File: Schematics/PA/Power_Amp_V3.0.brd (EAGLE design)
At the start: 50.5 x 78.1 mm, 109 parts, among them J1 4_PIN_AMPCONN, J10 OSTVN03A150, J11 OSTVN03A150, J12 OSTVN03A150, J13 OSTVN03A150, J14 OSTVN03A150, J2 1984633, J3 2TERMINAL_SPEAKER, J4 2TERMINAL_SPEAKER, J5 2TERMINAL_SPEAKER, J6 OSTVN03A150, J7 OSTVN03A150, J8 OSTVN03A150, J9 OSTVN03A150, U1 LME49830, U2 LME49830, U3 LME49830

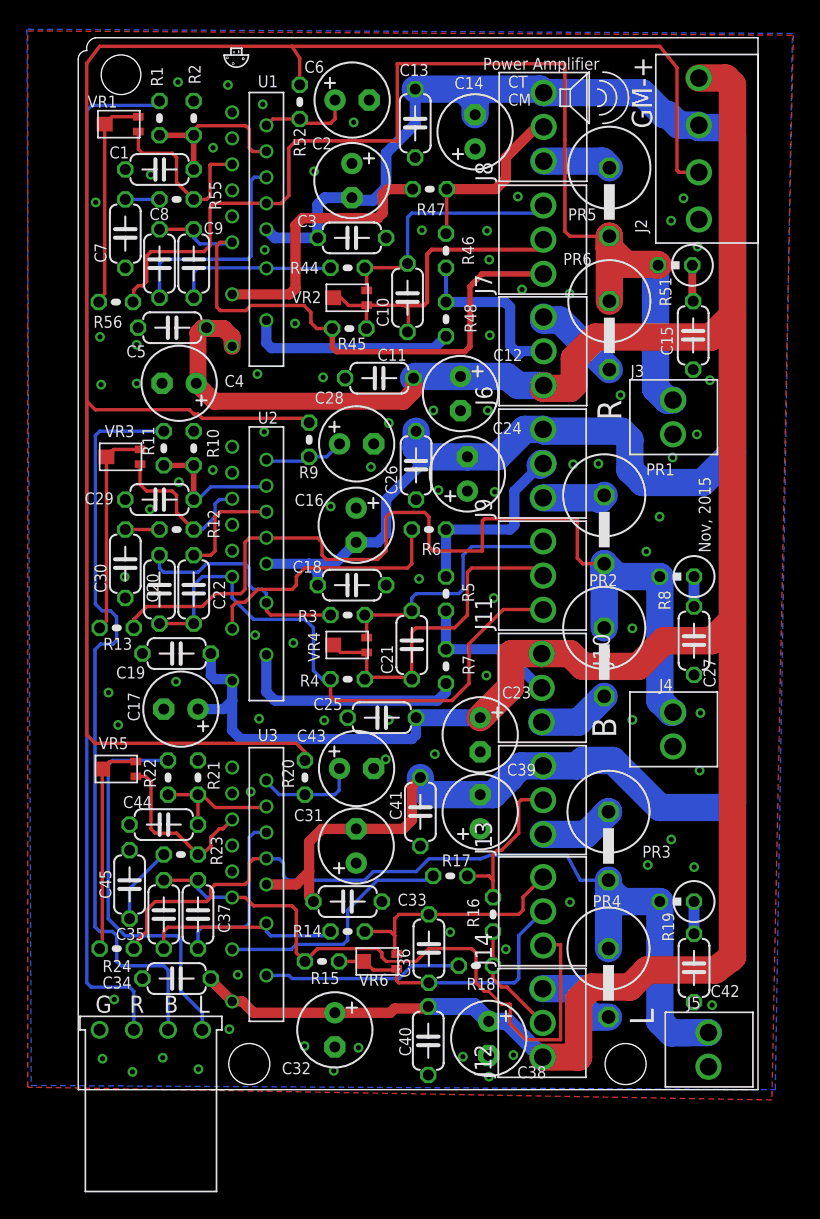
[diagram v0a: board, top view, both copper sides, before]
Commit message: small changes to silk screen
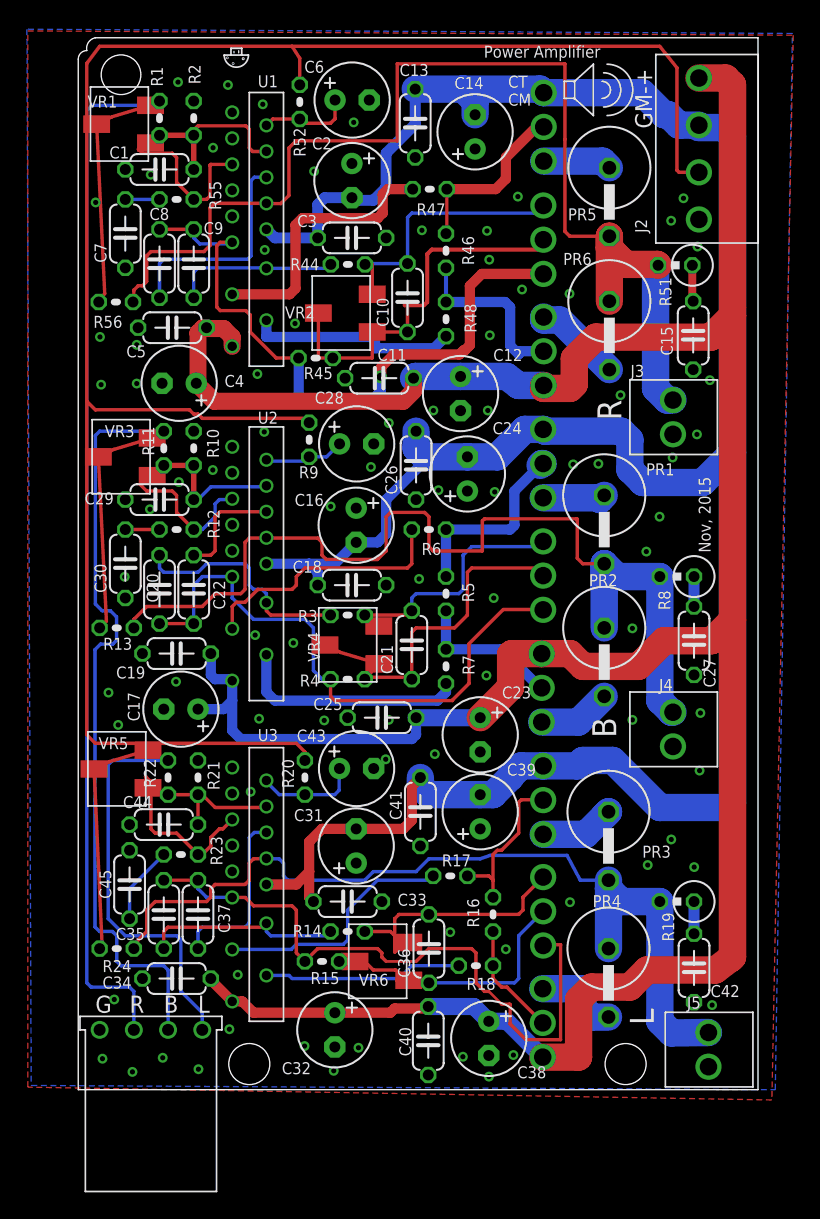
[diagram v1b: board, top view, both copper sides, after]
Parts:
- VR1, VR2, VR3, VR4, VR5, VR6: value (none) -> 23BR10KLFTR; device Amplifier_Parts:EVM2W -> Amplifier_Parts:23BR10KLFTR
- moved R45 3.32 mm to (17.6, 54.3)
- moved VR2 1.24 mm to (19.8, 57.7)
- moved U$48 0.66 mm to (35.6, 74.2)
- moved R44 0.26 mm to (20.0, 61.3)
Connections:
- net B_VBE_B: now also VR4.1, VR4.2; no longer VR4.A, VR4.B
- net B_VBE_C: now also VR4.3; no longer VR4.C
- net L_VBE_B: now also VR6.1, VR6.2; no longer VR6.A, VR6.B
- net L_VBE_C: now also VR6.3; no longer VR6.C
- net N$19: now also VR3.1; no longer VR3.A
- net N$20: now also VR3.2, VR3.3; no longer VR3.B, VR3.C
- net N$31: now also VR1.1; no longer VR1.A
- net N$40: now also VR1.2, VR1.3; no longer VR1.B, VR1.C
- net N$42: now also VR5.1; no longer VR5.A
- net N$43: now also VR5.2, VR5.3; no longer VR5.B, VR5.C
- net R_VBE_B: now also VR2.1, VR2.2; no longer VR2.A, VR2.B
- net R_VBE_C: now also VR2.3; no longer VR2.C
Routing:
- net R_VBE_E: track 44.3 -> 49.2 mm, vias 0 -> 1
- net R_VBE_B: track 24.2 -> 28.6 mm
- net N$20: track 15.6 -> 17.2 mm
- net N$40: track 16.1 -> 17.6 mm
- net N$43: track 16.1 -> 17.7 mm
- net L_VBE_B: track 20.4 -> 21.6 mm
- net L_VBE_C: track 17.9 -> 19.0 mm
- net B_VBE_B: track 25.5 -> 26.5 mm
- net R_VBE_C: track 19.3 -> 20.2 mm
